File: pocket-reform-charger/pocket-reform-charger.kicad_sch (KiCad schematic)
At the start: 74 parts, among them J1 CHARGER, Q3 Q_Dual_NMOS_S1G1S2G2D2D2D1D1, U1 MP2650, U2 MAX17320G20+, U3 NX20P5090

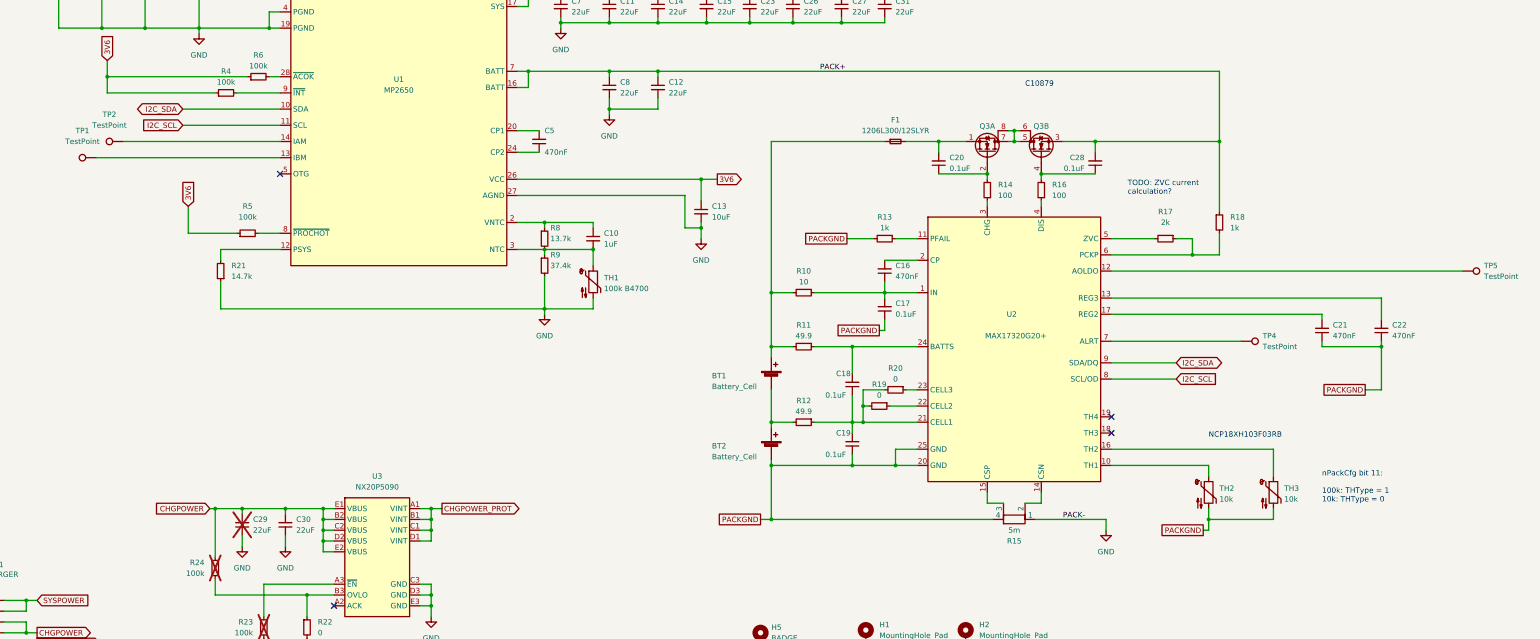
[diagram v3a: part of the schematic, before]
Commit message: charger v2: bom tweaks
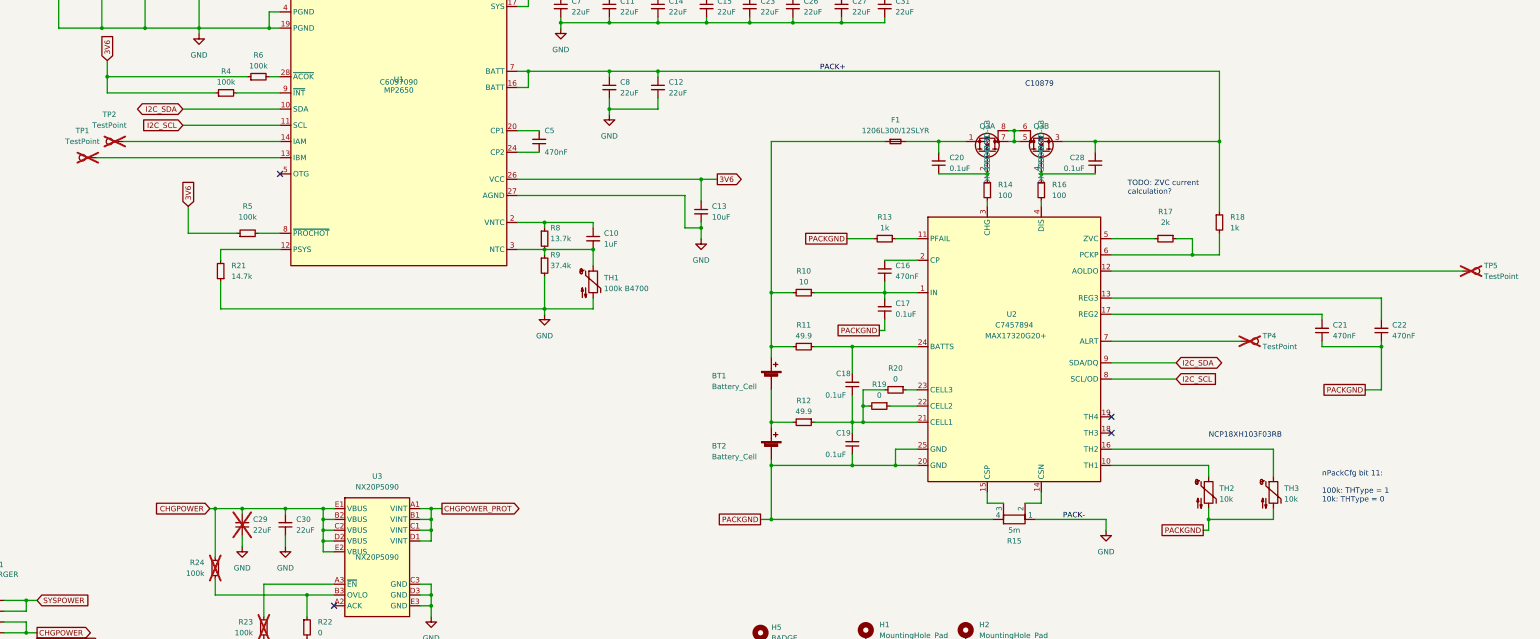
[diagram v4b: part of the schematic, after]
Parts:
- Q3: Digikey DMG9926USD-13DICT-ND -> (none); LCSC (none) -> C154896; MPN DMG9926USD-13 -> (none); Manufacturer_No (none) -> DMG9926USD-13
- R12: Manufacturer_No CRCW120649R9FKEAHP -> CRCW120649R9FKEAHP
- TP1, TP2, TP4, TP5: now not fitted; now left out of the parts list
- U1: LCSC (none) -> C6097090; Manufacturer_No MP2650 -> MP2650GV-0000-Z
- U2: LCSC (none) -> C7457894
- U3: LCSC (none) -> NX20P5090UKAZ; Manufacturer (none) -> NXP; Manufacturer_No (none) -> NX20P5090
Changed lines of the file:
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@@
 			)
 		)
-		(property "Digikey" ""
+		(property "Manufacturer" "NXP"
 			(at 134.62 240.03 0)
 			(effects
@@
 			)
 		)
-		(property "Manufacturer" ""
+		(property "DNP" ""
 			(at 134.62 240.03 0)
 			(effects
@@
 					(size 1.27 1.27)
 				)
-				(hide yes)
 			)
 		)
-		(property "MPN" ""
+		(property "LCSC" "NX20P5090UKAZ"
 			(at 134.62 240.03 0)
 			(effects
@@
 			)
 		)
-		(property "DNP" ""
+		(property "Manufacturer_No" "NX20P5090"
 			(at 134.62 240.03 0)
 			(effects
@@
 			)
 		)
-		(property "LCSC" ""
-			(at 134.62 240.03 0)
-			(effects
-				(font
-					(size 1.27 1.27)
-				)
-				(hide yes)
-			)
-		)
 		(pin "E1"
 		)
@@
 			)
 		)
-		(property "Digikey" ""
-			(at 113.03 232.41 0)
-			(effects
-				(font
-					(size 1.27 1.27)
-				)
-				(hide yes)
-			)
-		)
-		(property "MPN" ""
-			(at 113.03 232.41 0)
-			(effects
-				(font
-					(size 1.27 1.27)
-				)
-				(hide yes)
-			)
-		)
 		(property "DNP" ""
 			(at 113.03 232.41 0)
@@
 			)
 		)
-		(property "Digikey" ""
-			(at 86.36 100.33 0)
-			(effects
-				(font
-					(size 1.27 1.27)
-				)
-				(hide yes)
-			)
-		)
-		(property "MPN" ""
-			(at 86.36 100.33 0)
-			(effects
-				(font
-					(size 1.27 1.27)
-				)
-				(hide yes)
-			)
-		)
 		(property "DNP" ""
 			(at 86.36 100.33 0)
@@
 			)
 		)
-		(property "Digikey" ""
-			(at 107.95 256.54 0)
-			(effects
-				(font
-					(size 1.27 1.27)
-				)
-				(hide yes)
-			)
-		)
-		(property "MPN" ""
-			(at 107.95 256.54 0)
-			(effects
-				(font
-					(size 1.27 1.27)
-				)
-				(hide yes)
-			)
-		)
 		(property "DNP" ""
 			(at 107.95 256.54 0)
@@
 			)
 		)
+		(property "LCSC" "C7457894"
+			(at 284.48 185.42 0)
+			(effects
+				(font
+					(size 1.27 1.27)
+				)
+			)
+		)
 		(pin "1"
 		)
@@
 			)
 		)
-		(property "Digikey" ""
-			(at 59.69 105.41 0)
-			(effects
-				(font
-					(size 1.27 1.27)
-				)
-				(hide yes)
-			)
-		)
-		(property "MPN" ""
-			(at 59.69 105.41 0)
-			(effects
-				(font
-					(size 1.27 1.27)
-				)
-				(hide yes)
-			)
-		)
 		(property "DNP" ""
 			(at 59.69 105.41 0)
@@
 			)
 		)
-		(property "Digikey" "DMG9926USD-13DICT-ND"
+		(property "Manufacturer" "Diodes Incorporated"
 			(at 278.13 144.78 0)
 			(effects
@@
 			)
 		)
-		(property "MPN" "DMG9926USD-13"
+		(property "Manufacturer_No" "DMG9926USD-13"
 			(at 278.13 144.78 0)
 			(effects
@@
 					(size 1.27 1.27)
 				)
-				(hide yes)
 			)
 		)
-		(property "Manufacturer" "Diodes Incorporated"
+		(property "LCSC" "C154896"
 			(at 278.13 144.78 0)
 			(effects
@@
 					(size 1.27 1.27)
 				)
-				(hide yes)
 			)
 		)
@@
 			)
 		)
-		(property "Digikey" ""
-			(at 69.85 105.41 0)
-			(effects
-				(font
-					(size 1.27 1.27)
-				)
-				(hide yes)
-			)
-		)
-		(property "MPN" ""
-			(at 69.85 105.41 0)
-			(effects
-				(font
-					(size 1.27 1.27)
-				)
-				(hide yes)
-			)
-		)
 		(property "DNP" ""
 			(at 69.85 105.41 0)
@@
 		(unit 1)
 		(exclude_from_sim no)
-		(in_bom yes)
+		(in_bom no)
 		(on_board yes)
-		(dnp no)
+		(dnp yes)
 		(fields_autoplaced yes)
 		(property "Reference" "TP5"
@@
 			)
 		)
-		(property "Digikey" ""
-			(at 102.87 232.41 0)
-			(effects
-				(font
-					(size 1.27 1.27)
-				)
-				(hide yes)
-			)
-		)
-		(property "MPN" ""
-			(at 102.87 232.41 0)
-			(effects
-				(font
-					(size 1.27 1.27)
-				)
-				(hide yes)
-			)
-		)
 		(property "DNP" ""
 			(at 102.87 232.41 0)
@@
 			)
 		)
-		(property "Manufacturer_No" "CRCW120649R9FKEAHP "
+		(property "Manufacturer_No" "CRCW120649R9FKEAHP"
 			(at 234.95 208.28 0)
 			(effects
@@
 		(unit 1)
 		(exclude_from_sim no)
-		(in_bom yes)
+		(in_bom no)
 		(on_board yes)
-		(dnp no)
+		(dnp yes)
 		(fields_autoplaced yes)
 		(property "Reference" "TP2"
@@
 		(unit 1)
 		(exclude_from_sim no)
-		(in_bom yes)
+		(in_bom no)
 		(on_board yes)
-		(dnp no)
+		(dnp yes)
 		(fields_autoplaced yes)
 		(property "Reference" "TP4"
@@
 			)
 		)
-		(property "Digikey" "DMG9926USD-13DICT-ND"
+		(property "Manufacturer" "Diodes Incorporated"
 			(at 290.83 144.78 0)
 			(effects
@@
 			)
 		)
-		(property "MPN" "DMG9926USD-13"
+		(property "Manufacturer_No" "DMG9926USD-13"
 			(at 290.83 144.78 0)
 			(effects
@@
 					(size 1.27 1.27)
 				)
-				(hide yes)
 			)
 		)
-		(property "Manufacturer" "Diodes Incorporated"
+		(property "LCSC" "C154896"
 			(at 290.83 144.78 0)
 			(effects
@@
 					(size 1.27 1.27)
 				)
-				(hide yes)
 			)
 		)
@@
 			)
 		)
-		(property "Manufacturer_No" "MP2650"
+		(property "Manufacturer_No" "MP2650GV-0000-Z"
 			(at 139.7 128.27 0)
 			(effects
@@
 			)
 		)
+		(property "LCSC" "C6097090"
+			(at 139.7 128.27 0)
+			(effects
+				(font
+					(size 1.27 1.27)
+				)
+			)
+		)
 		(pin "1"
 		)
@@
 			)
 		)
-		(property "Digikey" ""
-			(at 96.52 242.57 0)
-			(effects
-				(font
-					(size 1.27 1.27)
-				)
-				(hide yes)
-			)
-		)
-		(property "MPN" ""
-			(at 96.52 242.57 0)
-			(effects
-				(font
-					(size 1.27 1.27)
-				)
-				(hide yes)
-			)
-		)
 		(property "DNP" ""
 			(at 96.52 242.57 0)
@@
 		(unit 1)
 		(exclude_from_sim no)
-		(in_bom yes)
+		(in_bom no)
 		(on_board yes)
-		(dnp no)
+		(dnp yes)
 		(fields_autoplaced yes)
 		(property "Reference" "TP1"
@@
 			(at 284.48 231.14 0)
 			(effects
-				(font
-					(size 1.27 1.27)
-				)
-				(hide yes)
-			)
-		)
-		(property "Digikey" ""
-			(at 284.48 231.14 0)
-			(effects
-				(font
-					(size 1.27 1.27)
-				)
-				(hide yes)
-			)
-		)
-		(property "MPN" ""
-			(at 284.48 231.14 0)
-			(effects

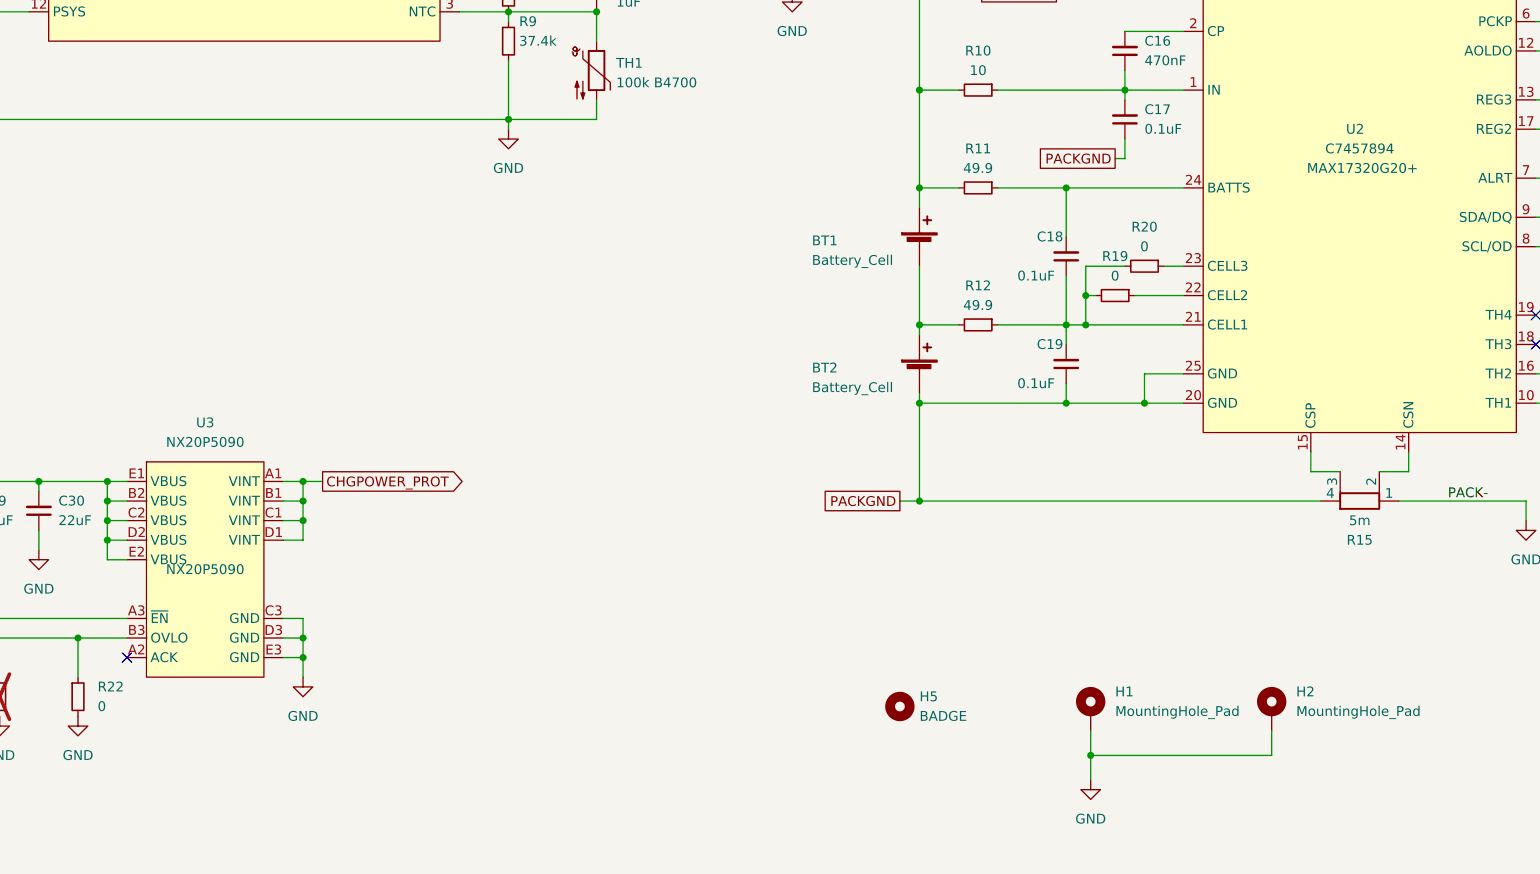
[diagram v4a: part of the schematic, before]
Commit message: pocket-reform-charger: update some part numbers for new batch
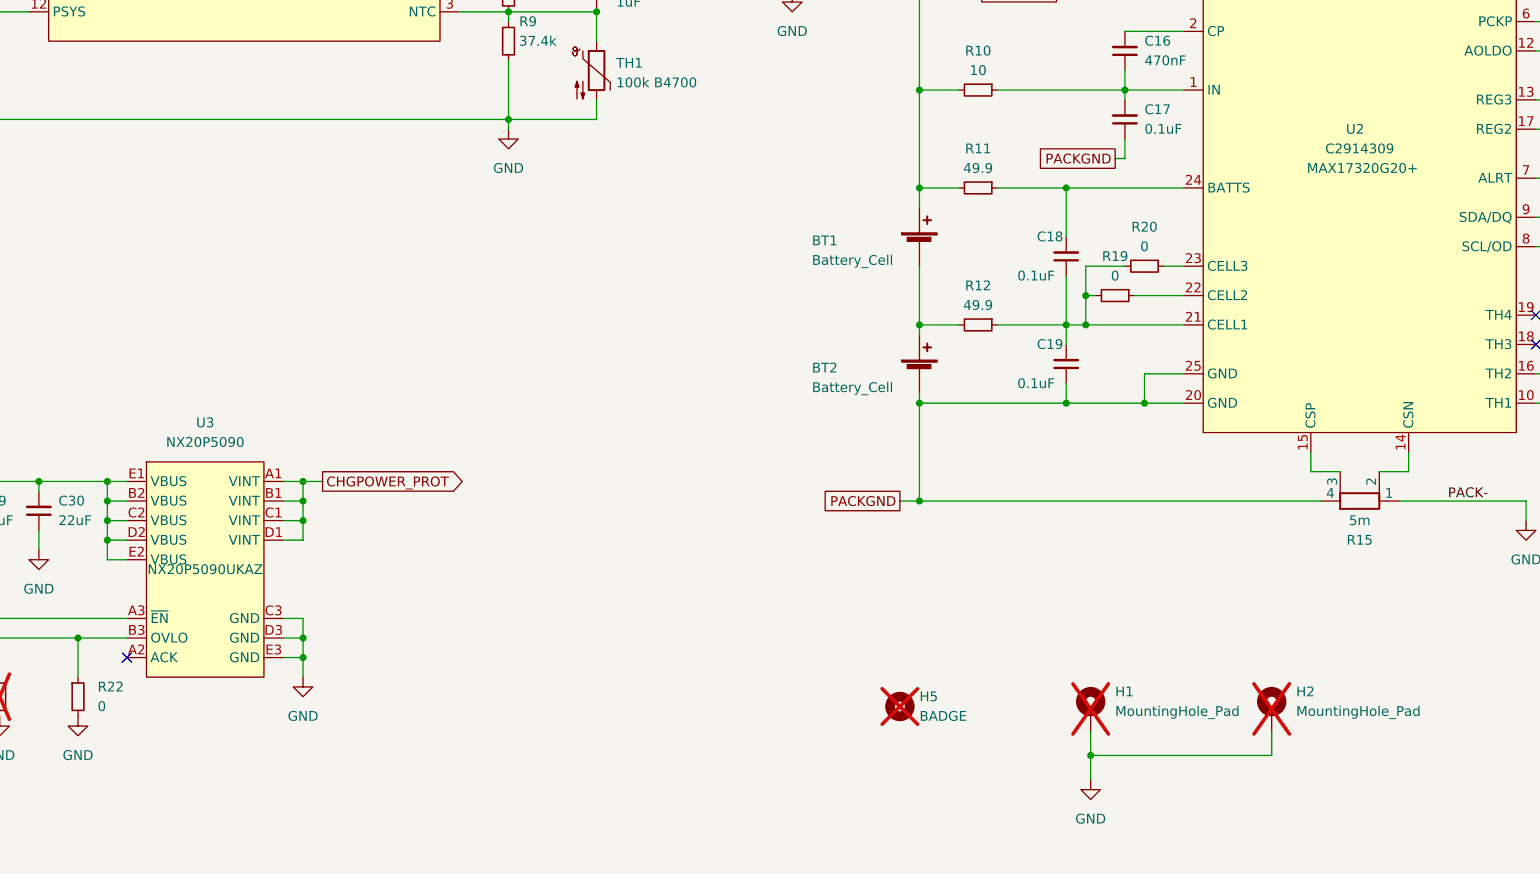
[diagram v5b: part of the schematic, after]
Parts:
- C17, C18, C19, C20, C28, C3, C9: LCSC C385964 -> C14663
- F1: LCSC C1512043 -> C1512052
- H1, H2, H5: now not fitted; now left out of the parts list
- J1: LCSC C278795 -> C395365
- R10: LCSC C193335 -> C22859
- R15: LCSC C2937388 -> C2988648
- R2, R3: LCSC C403469 -> C22977
- R21: LCSC C100775 -> C22874
- R8: LCSC C203293 -> C22793
- R9: LCSC C203565 -> C23033
- TH1: LCSC C153015 -> C14663
- U2: LCSC C7457894 -> C2914309
- U3: LCSC NX20P5090UKAZ -> C2802659; Manufacturer_No NX20P5090 -> NX20P5090UKAZ
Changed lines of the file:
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@@
 			)
 		)
-		(property "LCSC" "C203293"
+		(property "LCSC" "C22793"
 			(at 173.99 165.1 0)
 			(effects
@@
 			)
 		)
-		(property "LCSC" "C385964"
+		(property "LCSC" "C14663"
 			(at 246.38 199.39 0)
 			(effects
@@
 			)
 		)
-		(property "LCSC" "NX20P5090UKAZ"
+		(property "LCSC" "C2802659"
 			(at 134.62 240.03 0)
 			(effects
@@
 			)
 		)
-		(property "Manufacturer_No" "NX20P5090"
+		(property "Manufacturer_No" "NX20P5090UKAZ"
 			(at 134.62 240.03 0)
 			(effects
@@
 			)
 		)
-		(property "LCSC" "C1512043"
+		(property "LCSC" "C1512052"
 			(at 256.54 142.24 0)
 			(effects
@@
 			)
 		)
-		(property "LCSC" "C7457894"
+		(property "LCSC" "C2914309"
 			(at 284.48 185.42 0)
 			(effects
@@
 			)
 		)
-		(property "LCSC" "C385964"
+		(property "LCSC" "C14663"
 			(at 303.53 147.32 0)
 			(effects
@@
 			)
 		)
-		(property "LCSC" "C403469"
+		(property "LCSC" "C22977"
 			(at 97.79 90.17 0)
 			(effects
@@
 			)
 		)
-		(property "LCSC" "C193335"
+		(property "LCSC" "C22859"
 			(at 234.95 177.8 0)
 			(effects
@@
 			)
 		)
-		(property "LCSC" "C403469"
+		(property "LCSC" "C22977"
 			(at 97.79 95.25 0)
 			(effects
@@
 			)
 		)
-		(property "LCSC" "C385964"
+		(property "LCSC" "C14663"
 			(at 102.87 92.71 0)
 			(effects
@@
 			)
 		)
-		(property "LCSC" "C100775"
+		(property "LCSC" "C22874"
 			(at 97.79 172.72 0)
 			(effects
@@
 			)
 		)
-		(property "LCSC" "C385964"
+		(property "LCSC" "C14663"
 			(at 246.38 213.36 0)
 			(effects
@@
 			)
 		)
-		(property "LCSC" "C385964"
+		(property "LCSC" "C14663"
 			(at 254 181.61 0)
 			(effects
@@
 			)
 		)
-		(property "LCSC" "C153015"
+		(property "LCSC" "C14663"
 			(at 185.42 175.26 0)
 			(effects
@@
 		(unit 1)
 		(exclude_from_sim no)
-		(in_bom yes)
+		(in_bom no)
 		(on_board yes)
-		(dnp no)
+		(dnp yes)
 		(fields_autoplaced yes)
 		(property "Reference" "H1"
@@
 			)
 		)
-		(property "LCSC" "C385964"
+		(property "LCSC" "C14663"
 			(at 266.7 147.32 0)
 			(effects
@@
 		(unit 1)
 		(exclude_from_sim no)
-		(in_bom yes)
+		(in_bom no)
 		(on_board yes)
-		(dnp no)
+		(dnp yes)
 		(fields_autoplaced yes)
 		(property "Reference" "H5"
@@
 		(unit 1)
 		(exclude_from_sim no)
-		(in_bom yes)
+		(in_bom no)
 		(on_board yes)
-		(dnp no)
+		(dnp yes)
 		(fields_autoplaced yes)
 		(property "Reference" "H2"
@@
 			)
 		)
-		(property "LCSC" "C278795"
+		(property "LCSC" "C395365"
 			(at 41.91 260.35 0)
 			(effects
@@
 			)
 		)
-		(property "LCSC" "C203565"
+		(property "LCSC" "C23033"
 			(at 173.99 171.45 0)
 			(effects
@@
 			)
 		)
-		(property "LCSC" "C2937388"
+		(property "LCSC" "C2988648"
 			(at 284.48 231.14 0)
 			(effects
@@
 			)
 		)
-		(property "LCSC" "C385964"
+		(property "LCSC" "C14663"
 			(at 180.34 93.98 0)
 			(effects
